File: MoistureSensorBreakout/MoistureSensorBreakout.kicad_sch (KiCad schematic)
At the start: 4 parts, among them J1 Conn_02x07_Odd_Even, J2 Conn_01x06, J3 Conn_01x05, J4 Conn_01x14

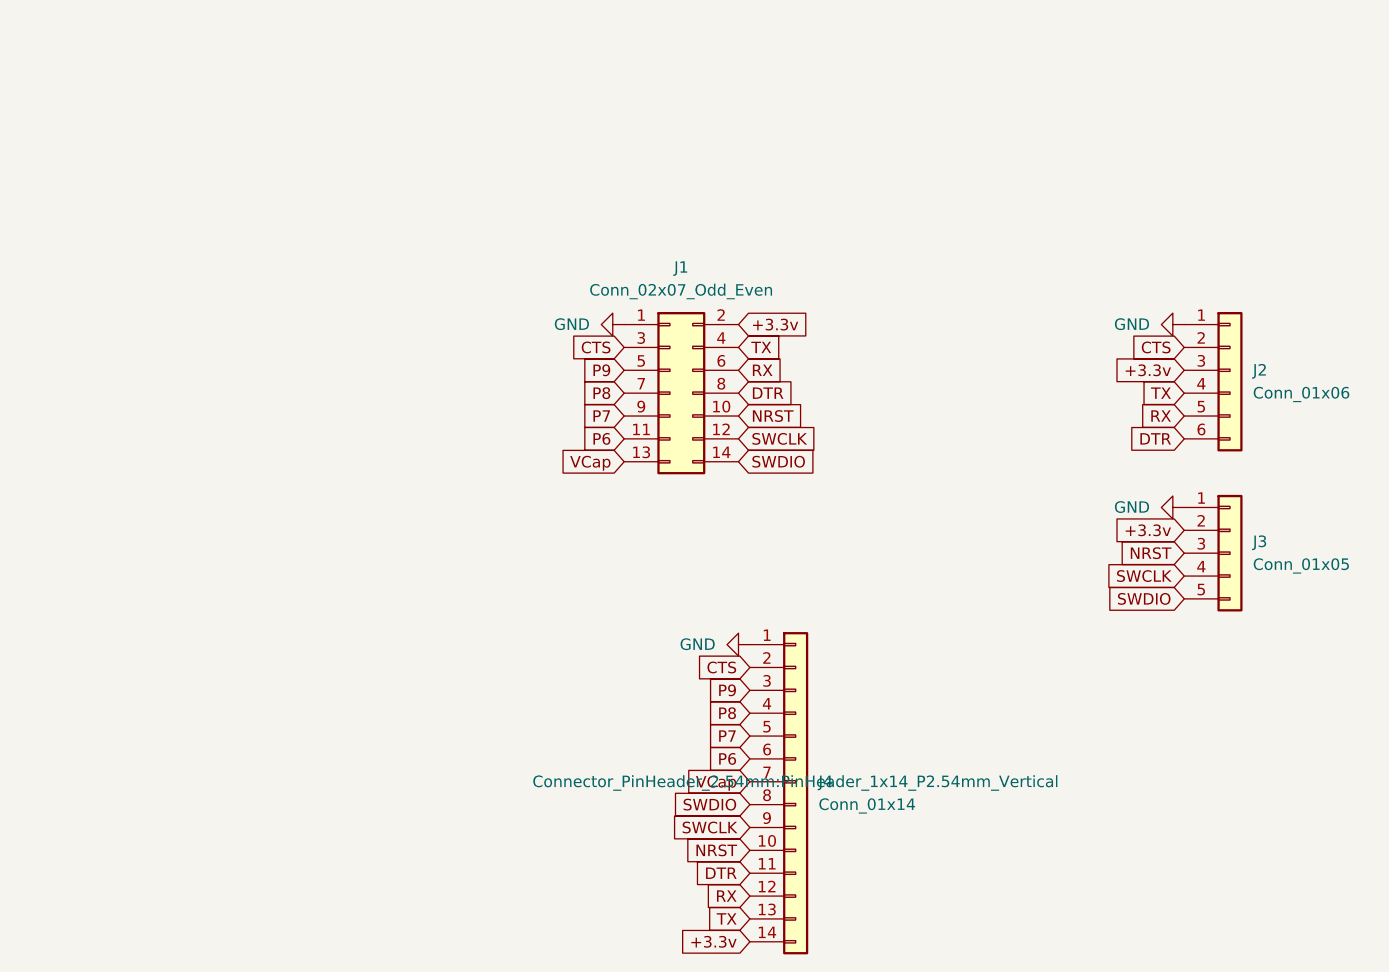
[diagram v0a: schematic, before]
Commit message: New version of breakout / programming board
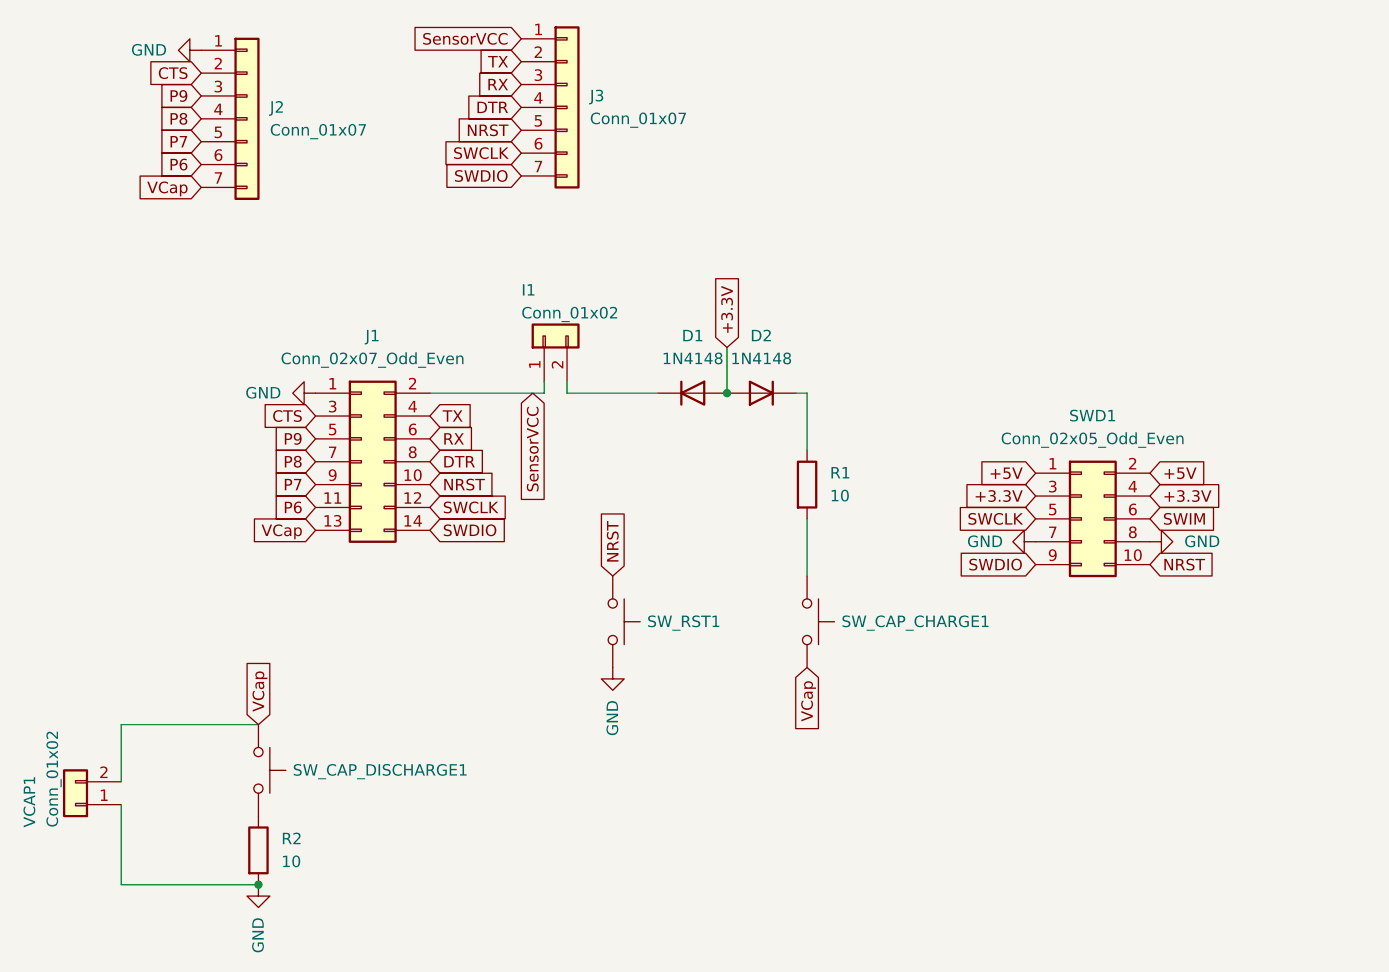
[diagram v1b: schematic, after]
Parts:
- removed J2: Conn_01x06, Connector_PinHeader_2.54mm:PinHeader_1x06_P2.54mm_Vertical, symbol Connector_Generic:Conn_01x06
- removed J3: Conn_01x05, Connector_PinHeader_2.54mm:PinHeader_1x05_P2.54mm_Vertical, symbol Connector_Generic:Conn_01x05
- removed J4: Conn_01x14, Connector_PinHeader_2.54mm:PinHeader_1x14_P2.54mm_Vertical, symbol Connector_Generic:Conn_01x14
- added D1, D2: 1N4148, Diode_THT:D_DO-35_SOD27_P7.62mm_Horizontal, symbol Diode:1N4148
- added I1, VCAP1: Conn_01x02, Connector_PinHeader_2.54mm:PinHeader_1x02_P2.54mm_Vertical, symbol Connector_Generic:Conn_01x02
- added J2, J3: Conn_01x07, Connector_PinHeader_2.54mm:PinHeader_1x07_P2.54mm_Vertical, symbol Connector_Generic:Conn_01x07
- added R1, R2: 10, Resistor_THT:R_Axial_DIN0207_L6.3mm_D2.5mm_P7.62mm_Horizontal, symbol Device:R
- added SWD1: Conn_02x05_Odd_Even, Connector_PinHeader_2.54mm:PinHeader_2x05_P2.54mm_Horizontal, symbol Connector_Generic:Conn_02x05_Odd_Even
- added SW_CAP_CHARGE1, SW_CAP_DISCHARGE1, SW_RST1: SW_Push, Button_Switch_THT:SW_PUSH_6mm, symbol Switch:SW_Push
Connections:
- net CTS: now also J2.2 (Pin_2)
- net DTR: now also J3.4 (Pin_4)
- net GND: now also J2.1 (Pin_1), R2.2, SWD1.7 (Pin_7), SWD1.8 (Pin_8), SW_RST1.2, VCAP1.1 (Pin_1)
- net NRST: now also J3.5 (Pin_5), SWD1.10 (Pin_10), SW_RST1.1
- net P6: now also J2.6 (Pin_6)
- net P7: now also J2.5 (Pin_5)
- net P8: now also J2.4 (Pin_4)
- net P9: now also J2.3 (Pin_3)
- net RX: now also J3.3 (Pin_3)
- net SWCLK: now also J3.6 (Pin_6), SWD1.5 (Pin_5)
- net SWDIO: now also J3.7 (Pin_7), SWD1.9 (Pin_9)
- net TX: now also J3.2 (Pin_2)
- net VCap: now also J2.7 (Pin_7), SW_CAP_CHARGE1.2, SW_CAP_DISCHARGE1.1, VCAP1.2 (Pin_2)
- net +3.3v renamed SensorVCC
- net SensorVCC: now also I1.1 (Pin_1), J3.1 (Pin_1)
- new net: D2.1 (K), R1.1
- new net: R1.2, SW_CAP_CHARGE1.1
- new net: D1.1 (K), I1.2 (Pin_2)
- new net: R2.1, SW_CAP_DISCHARGE1.2
- new net +3.3V: D1.2 (A), D2.2 (A), SWD1.3 (Pin_3), SWD1.4 (Pin_4)
- new net +5V: SWD1.1 (Pin_1), SWD1.2 (Pin_2)
- new net SWIM: SWD1.6 (Pin_6)
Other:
- moved on the sheet: J1
